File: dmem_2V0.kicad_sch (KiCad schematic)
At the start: 6 parts, among them J1 D15P33E4GV00LF, J10 7701-3, J11 7701-3

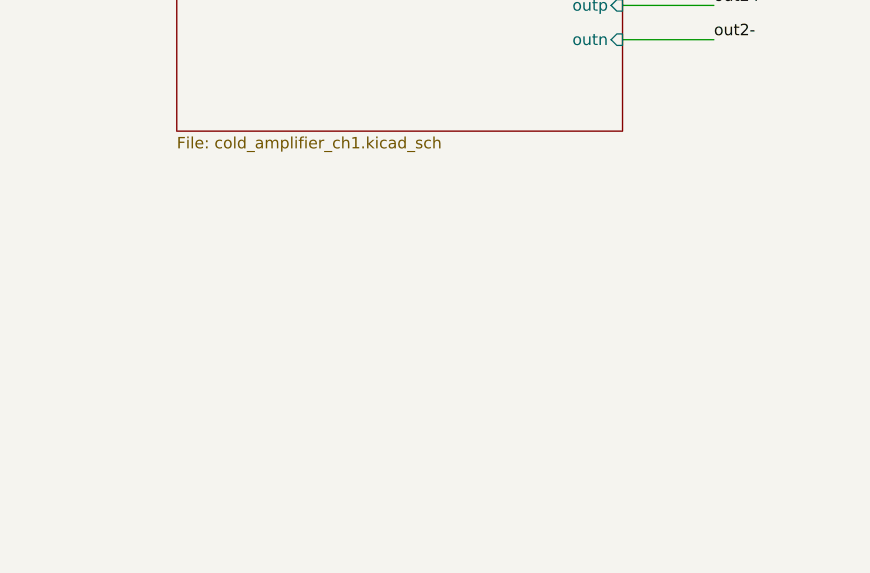
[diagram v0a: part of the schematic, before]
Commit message: Added jumpers to connect ground to mounting holes to ground
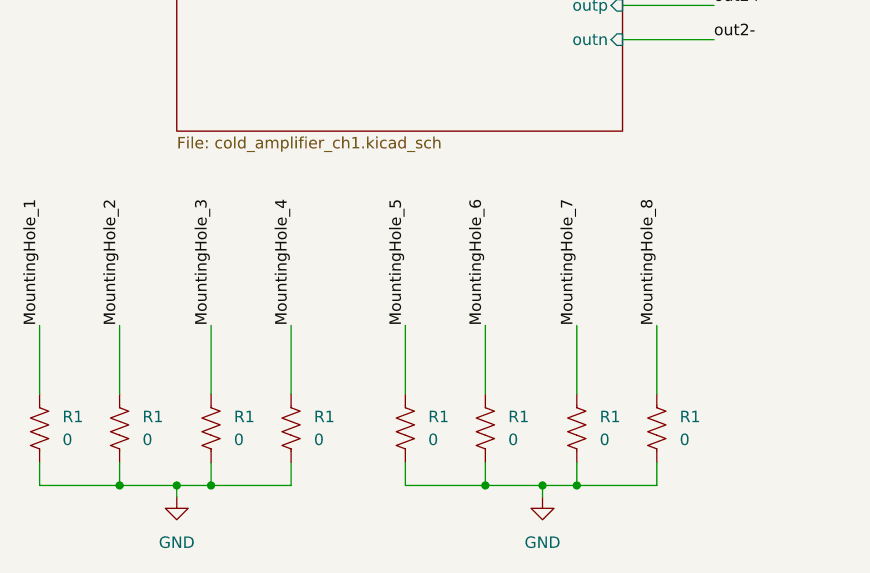
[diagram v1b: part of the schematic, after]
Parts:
- added R1 (x8): 0, Resistor_SMD:R_0805_2012Metric, symbol Device:R_US
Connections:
- net GND: now also R1.1, R1.1, R1.1, R1.1, R1.1, R1.1, R1.1, R1.1
- new net MountingHole_1: R1.2
- new net MountingHole_2: R1.2
- new net MountingHole_3: R1.2
- new net MountingHole_4: R1.2
- new net MountingHole_5: R1.2
- new net MountingHole_6: R1.2
- new net MountingHole_7: R1.2
- new net MountingHole_8: R1.2

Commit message: DMEM combination
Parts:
- added J12: D15S33E4GV00LF, User_footprints:AMPHENOL_D15S33E4GV00LF, symbol D15S33E4GV00LF:D15S33E4GV00LF
- added JP1: Jumper_2_Open, Resistor_SMD:R_1206_3216Metric, symbol Jumper:Jumper_2_Open
- added R1: 0, Resistor_SMD:R_0603_1608Metric, symbol Device:R_US
- J1: Digikey Part Number (none) -> 609-1492-ND; Part Number (none) -> D15P33E4GV00LF
- J10: Digikey Part Number (none) -> 36-7701-3-ND; Part Number  (none) -> 7701-3
- J11: footprint User_footprints:KEYSTONE_7701-3 -> 7701-3:KEYSTONE_7701-3; Description  (none) -> 4 Pin Screw Terminal, Power Tap 6-32 Through Hole; Digikey Part Number (none) -> 36-7701-3-ND; Part Number  (none) -> 7701-3
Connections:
- net +CE: now also J12.5
- net +CE_R: now also J12.14
- net GND: now also J12.15, J12.6, J12.7, J12.8, R1.1
- net MESH: now reaches J10.1_1 (1), J10.1_2 (1__1), J10.1_3 (1__2), J10.1_4 (1__3), JP2.1 (A), JP3.2 (B)
- net MESH: now also JP1.2 (B)
- net at JP3.1 (A): now also J1.S1 (SHIELD); no longer J1.16
- net out2_jumper-: now reaches J1.1
- net out2_jumper-: now also J12.3
- net out1_jumper+: now reaches J1.10
- net out1_jumper+: now also J12.12
- net out1_jumper-: now reaches J1.2
- net out1_jumper-: now also J12.4
- net out2_jumper+: now reaches J1.9
- net out2_jumper+: now also J12.11
- new net: J12.13, R1.2
- new net: J12.S1 (SHIELD), JP1.1 (A)
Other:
- moved on the sheet: JP3, R1

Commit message: Moved connectors SiPM flex connectorsto both sides; rectangular vias stitching pattern
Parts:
- J1: MANUFACTURER Amphenol ICC (FCI) -> (none); Manufacturer (none) -> Amphenol ICC (FCI)
- J10: MANUFACTURER Keystone Electronics -> (none); Manufacturer (none) -> Keystone Electronics
- J12: Digikey Part Number (none) -> 609-1498-ND; MANUFACTURER Amphenol -> (none); Manufacturer (none) -> Amphenol ICC (FCI); Part Number (none) -> D15S33E4GV00LF
- JP1, JP2, JP3: Digikey Part Number (none) -> RMCF1206ZT0R00CT-ND; Manufacturer (none) -> Stackpole Electronics Inc; Part Number (none) -> RMCF1206ZT0R00
- R1: Digikey Part Number (none) -> 749-MCU0805MZ0000ZP500CT-ND; Manufacturer (none) -> Vishay Beyschlag/Draloric/BC Components; Part Number (none) -> MCU0805MZ0000ZP500

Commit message: completed BOM list; replaced 47u with 33u capacitor
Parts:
- J1: MAXIMUM_PACKAGE_HEIGHT 12.96mm -> (none); PARTREV D -> (none); STANDARD Manufacturer recommendations -> (none)
- J10: footprint User_footprints:KEYSTONE_7701-3 -> 7701-3:KEYSTONE_7701-3; MAXIMUM_PACKAGE_HEIGHT 5.33 mm -> (none); PARTREV G -> (none); Part Number (none) -> 7701-3; Part Number  7701-3 -> (none); STANDARD Manufacturer Recommendations -> (none)
- J11: Description  4 Pin Screw Terminal, Power Tap 6-32 Through Hole -> (none); MANUFACTURER Keystone Electronics -> (none); MAXIMUM_PACKAGE_HEIGHT 5.33 mm -> (none); Manufacturer (none) -> Keystone Electronics; PARTREV G -> (none); Part Number (none) -> 7701-3; Part Number  7701-3 -> (none); STANDARD Manufacturer Recommendations -> (none)
- J12: footprint User_footprints:AMPHENOL_D15S33E4GV00LF -> D15S33E4GV00LF:AMPHENOL_D15S33E4GV00LF; PARTREV D -> (none); SNAPEDA_PN D15S33E4GV00LF -> (none); STANDARD Manufacturer Recommendations -> (none)
- R1: Digikey Part Number (none) -> 749-MCU0805MZ0000ZP500CT-ND; Manufacturer (none) -> Vishay Beyschlag/Draloric/BC Components; Part Number (none) -> MCU0805MZ0000ZP500
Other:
- moved on the sheet: J1
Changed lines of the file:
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@@
-    (stroke (width 0) (type default))
-  )
-  (wire (pts (xy 187.96 110.49) (xy 187.96 115.57))
     (stroke (width 0) (type default))
   )
@@
   )
   (wire (pts (xy 116.84 140.97) (xy 116.84 148.59))
+    (stroke (width 0) (type default))
+  )
+  (wire (pts (xy 187.96 111.76) (xy 187.96 115.57))
     (stroke (width 0) (type default))
   )
@@
       (effects (font (size 1.27 1.27)) hide)
     )
-    (property "PARTREV" "G" (at 251.46 143.51 0)
+    (property "Manufacturer" "Keystone Electronics" (at 251.46 138.43 0)
       (effects (font (size 1.27 1.27)) (justify bottom) hide)
     )
-    (property "STANDARD" "Manufacturer Recommendations" (at 251.46 143.51 0)
-      (effects (font (size 1.27 1.27)) (justify bottom) hide)
-    )
-    (property "MAXIMUM_PACKAGE_HEIGHT" "5.33 mm" (at 251.46 143.51 0)
-      (effects (font (size 1.27 1.27)) (justify bottom) hide)
-    )
-    (property "MANUFACTURER" "Keystone Electronics" (at 251.46 143.51 0)
-      (effects (font (size 1.27 1.27)) (justify bottom) hide)
-    )
-    (property "Part Number " "7701-3" (at 251.46 143.51 0)
+    (property "Part Number" "7701-3" (at 251.46 143.51 0)
       (effects (font (size 1.27 1.27)) hide)
     )
@@
       (effects (font (size 1.27 1.27)) hide)
     )
-    (property "Description " "4 Pin Screw Terminal, Power Tap 6-32 Through Hole" (at 251.46 143.51 0)
+    (property "Description" "4 Pin Screw Terminal, Power Tap 6-32 Through Hole" (at 251.46 143.51 0)
       (effects (font (size 1.27 1.27)) hide)
     )
@@
       (effects (font (size 1.27 1.27)))
     )
-    (property "Footprint" "User_footprints:AMPHENOL_D15S33E4GV00LF" (at 199.39 36.83 0)
+    (property "Footprint" "D15S33E4GV00LF:AMPHENOL_D15S33E4GV00LF" (at 199.39 36.83 0)
       (effects (font (size 1.27 1.27)) (justify bottom) hide)
     )
@@
       (effects (font (size 1.27 1.27)) hide)
     )
-    (property "PARTREV" "D" (at 200.66 55.88 0)
-      (effects (font (size 1.27 1.27)) (justify bottom) hide)
-    )
-    (property "STANDARD" "Manufacturer Recommendations" (at 172.72 44.45 0)
-      (effects (font (size 1.27 1.27)) (justify bottom) hide)
-    )
-    (property "SNAPEDA_PN" "D15S33E4GV00LF" (at 172.72 48.26 0)
-      (effects (font (size 1.27 1.27)) (justify bottom) hide)
-    )
-    (property "Manufacturer" "Amphenol ICC (FCI)" (at 180.34 41.91 0)
-      (effects (font (size 1.27 1.27)) (justify bottom) hide)
+    (property "Manufacturer" "Amphenol ICC (FCI)" (at 200.66 55.88 0)
+      (effects (font (size 1.27 1.27)) hide)
     )
     (property "Part Number" "D15S33E4GV00LF" (at 200.66 55.88 0)
@@
       (effects (font (size 1.27 1.27)) hide)
     )
+    (pin "10")
+    (pin "11")
+    (pin "12")
+    (pin "13")
+    (pin "14")
+    (pin "15")
+    (pin "S1")
     (pin "1")
     (pin "2")
@@
     (pin "8")
     (pin "9")
-    (pin "10")
-    (pin "11")
-    (pin "12")
-    (pin "13")
-    (pin "14")
-    (pin "15")
-    (pin "S1")
     (instances
       (project "dmem_2V0"
@@
       (effects (font (size 1.27 1.27)) hide)
     )
+    (property "Manufacturer" "Vishay Beyschlag/Draloric/BC Components" (at 231.14 55.88 0)
+      (effects (font (size 1.27 1.27)) hide)
+    )
+    (property "Part Number" "MCU0805MZ0000ZP500" (at 231.14 55.88 0)
+      (effects (font (size 1.27 1.27)) hide)
+    )
+    (property "Digikey Part Number" "749-MCU0805MZ0000ZP500CT-ND" (at 231.14 55.88 0)
+      (effects (font (size 1.27 1.27)) hide)
+    )
+    (property "Description" "0 Ohms Jumper Chip Resistor 0805 (2012 Metric) Anti-Sulfur, Automotive AEC-Q200 Thin Film" (at 231.14 55.88 0)
+      (effects (font (size 1.27 1.27)) hide)
+    )
     (pin "1")
     (pin "2")
@@
     )
   )
-  (symbol (lib_name "7701-3_1") (lib_id "7701-3:7701-3") (at 251.46 127 0) (unit 1)
+  (symbol (lib_id "7701-3:7701-3") (at 251.46 127 0) (unit 1)
     (in_bom yes) (on_board yes) (dnp no) (fields_autoplaced)
     (property "Reference" "J10" (at 257.81 129.54 0)
@@
       (effects (font (size 1.27 1.27)) (justify left))
     )
-    (property "Footprint" "User_footprints:KEYSTONE_7701-3" (at 251.46 127 0)
+    (property "Footprint" "7701-3:KEYSTONE_7701-3" (at 251.46 127 0)
       (effects (font (size 1.27 1.27)) (justify bottom) hide)
     )
@@
       (effects (font (size 1.27 1.27)) hide)
     )
-    (property "PARTREV" "G" (at 251.46 127 0)
+    (property "Manufacturer" "Keystone Electronics" (at 251.46 121.92 0)
       (effects (font (size 1.27 1.27)) (justify bottom) hide)
     )
-    (property "STANDARD" "Manufacturer Recommendations" (at 251.46 127 0)
-      (effects (font (size 1.27 1.27)) (justify bottom) hide)
-    )
-    (property "MAXIMUM_PACKAGE_HEIGHT" "5.33 mm" (at 251.46 127 0)
-      (effects (font (size 1.27 1.27)) (justify bottom) hide)
-    )
-    (property "Manufacturer" "Keystone Electronics" (at 251.46 127 0)
-      (effects (font (size 1.27 1.27)) (justify bottom) hide)
-    )
-    (property "Part Number " "7701-3" (at 251.46 127 0)
+    (property "Part Number" "7701-3" (at 251.46 127 0)
       (effects (font (size 1.27 1.27)) hide)
     )
@@
       (effects (font (size 1.27 1.27)) hide)
     )
-    (property "PARTREV" "D" (at 200.66 96.52 0)
-      (effects (font (size 1.27 1.27)) (justify bottom) hide)
-    )
-    (property "MAXIMUM_PACKAGE_HEIGHT" "12.96mm" (at 168.91 90.17 0)
-      (effects (font (size 1.27 1.27)) (justify bottom) hide)
-    )
-    (property "STANDARD" "Manufacturer recommendations" (at 177.8 80.01 0)
-      (effects (font (size 1.27 1.27)) (justify bottom) hide)
-    )
-    (property "Manufacturer" "Amphenol ICC (FCI)" (at 166.37 93.98 0)
-      (effects (font (size 1.27 1.27)) (justify bottom) hide)
-    )
-    (property "Part Number" "D15P33E4GV00LF" (at 214.63 80.01 0)
-      (effects (font (size 1.27 1.27)) hide)
-    )
-    (property "Digikey Part Number" "609-1492-ND" (at 209.55 76.2 0)
-      (effects (font (size 1.27 1.27)) hide)
-    )
-    (property "Description" "15 Position D-Sub Plug, Male Pins Connector" (at 215.9 72.39 0)
+    (property "Manufacturer" "Amphenol ICC (FCI)" (at 179.07 83.82 0)
+      (effects (font (size 1.27 1.27)) hide)
+    )
+    (property "Part Number" "D15P33E4GV00LF" (at 200.66 81.28 0)
+      (effects (font (size 1.27 1.27)) hide)
+    )
+    (property "Digikey Part Number" "609-1492-ND" (at 223.52 83.82 0)
+      (effects (font (size 1.27 1.27)) hide)
+    )
+    (property "Description" "15 Position D-Sub Plug, Male Pins Connector" (at 200.66 73.66 0)
       (effects (font (size 1.27 1.27)) hide)
     )
@@
       (effects (font (size 1.27 1.27)) hide)
     )
+    (property "Manufacturer" "Vishay Beyschlag/Draloric/BC Components" (at 231.14 99.06 0)
+      (effects (font (size 1.27 1.27)) hide)
+    )
+    (property "Part Number" "MCU0805MZ0000ZP500" (at 231.14 99.06 0)
+      (effects (font (size 1.27 1.27)) hide)
+    )
+    (property "Digikey Part Number" "749-MCU0805MZ0000ZP500CT-ND" (at 231.14 99.06 0)
+      (effects (font (size 1.27 1.27)) hide)
+    )
+    (property "Description" "0 Ohms Jumper Chip Resistor 0805 (2012 Metric) Anti-Sulfur, Automotive AEC-Q200 Thin Film" (at 231.14 99.06 0)
+      (effects (font (size 1.27 1.27)) hide)
+    )

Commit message: Adding test points and arrows to DB15s
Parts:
- added Vce1, Vce_r1: TestPoint, TestPoint:TestPoint_THTPad_1.0x1.0mm_Drill0.5mm, symbol Connector:TestPoint
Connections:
- net +CE: now also Vce1.1
- net +CE_R: now also Vce_r1.1
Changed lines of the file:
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@@
+    (stroke (width 0) (type default))
+  )
+  (wire (pts (xy 147.32 135.89) (xy 147.32 140.97))
     (stroke (width 0) (type default))
   )
@@
     (stroke (width 0) (type default))
   )
+  (wire (pts (xy 162.56 135.89) (xy 162.56 140.97))
+    (stroke (width 0) (type default))
+  )
   (wire (pts (xy 213.36 93.98) (xy 217.17 93.98))
     (stroke (width 0) (type default))
@@
     (effects (font (size 1.27 1.27)) (justify right bottom))
   )
+  (label "+CE_R" (at 162.56 140.97 180) (fields_autoplaced)
+    (effects (font (size 1.27 1.27)) (justify right bottom))
+  )
   (label "MountingHole_4" (at 76.2 140.97 90) (fields_autoplaced)
     (effects (font (size 1.27 1.27)) (justify left bottom))
@@
   )
   (label "out2-" (at 184.15 93.98 180) (fields_autoplaced)
+    (effects (font (size 1.27 1.27)) (justify right bottom))
+  )
+  (label "+CE" (at 147.32 140.97 180) (fields_autoplaced)
     (effects (font (size 1.27 1.27)) (justify right bottom))
   )
@@
     )
   )
+  (symbol (lib_id "Connector:TestPoint") (at 147.32 135.89 0) (unit 1)
+    (in_bom no) (on_board yes) (dnp no) (fields_autoplaced)
+    (property "Reference" "Vce1" (at 149.86 131.318 0)
+      (effects (font (size 1.27 1.27)) (justify left))
+    )
+    (property "Value" "TestPoint" (at 149.86 133.858 0)
+      (effects (font (size 1.27 1.27)) (justify left))
+    )
+    (property "Footprint" "TestPoint:TestPoint_THTPad_1.0x1.0mm_Drill0.5mm" (at 152.4 135.89 0)
+      (effects (font (size 1.27 1.27)) hide)
+    )
+    (property "Datasheet" "~" (at 152.4 135.89 0)
+      (effects (font (size 1.27 1.27)) hide)
+    )
+    (pin "1")
+    (instances
+      (project "dmem_2V0"
+        (path "/3e9c66f9-4dd4-413a-a9f0-4be475bcdd89"
+          (reference "Vce1") (unit 1)
+        )
+      )
+    )
+  )
   (symbol (lib_id "power:GND") (at 104.14 160.02 0) (unit 1)
     (in_bom yes) (on_board yes) (dnp no) (fields_autoplaced)
@@
         )
       )
+    )
+  )
+  (symbol (lib_id "Connector:TestPoint") (at 162.56 135.89 0) (unit 1)
+    (in_bom no) (on_board yes) (dnp no) (fields_autoplaced)
+    (property "Reference" "Vce_r1" (at 165.1 131.318 0)
+      (effects (font (size 1.27 1.27)) (justify left))
+    )
+    (property "Value" "TestPoint" (at 165.1 133.858 0)
+      (effects (font (size 1.27 1.27)) (justify left))
+    )
+    (property "Footprint" "TestPoint:TestPoint_THTPad_1.0x1.0mm_Drill0.5mm" (at 167.64 135.89 0)
+      (effects (font (size 1.27 1.27)) hide)
+    )
+    (property "Datasheet" "~" (at 167.64 135.89 0)
+      (effects (font (size 1.27 1.27)) hide)
+    )
+    (pin "1")
+    (instances
+      (project "dmem_2V0"
+        (path "/3e9c66f9-4dd4-413a-a9f0-4be475bcdd89"
+          (reference "Vce_r1") (unit 1)
+        )
+      )

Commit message: Solved error in netlist; input connector was in a mirror configuration; solved also DB15 error in netlist
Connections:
- net out1+: now also J1.4; no longer J1.12
- net out1-: now also J1.12; no longer J1.4
- net out1_jumper+: now also J1.2, J12.4; no longer J1.10, J12.12
- net out1_jumper-: now also J1.10, J12.12; no longer J1.2, J12.4
- net out2+: now also J1.3; no longer J1.11
- net out2-: now also J1.11; no longer J1.3
- net out2_jumper+: now also J1.1, J12.3; no longer J1.9, J12.11
- net out2_jumper-: now also J1.9, J12.11; no longer J1.1, J12.3
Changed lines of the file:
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@@
     (effects (font (size 1.27 1.27)) (justify left bottom))
   )
-  (label "out1_jumper+" (at 217.17 91.44 0) (fields_autoplaced)
+  (label "out1_jumper-" (at 217.17 91.44 0) (fields_autoplaced)
     (effects (font (size 1.27 1.27)) (justify left bottom))
   )
@@
     (effects (font (size 1.27 1.27)) (justify left bottom))
   )
-  (label "out2+" (at 217.17 93.98 0) (fields_autoplaced)
+  (label "out2-" (at 217.17 93.98 0) (fields_autoplaced)
     (effects (font (size 1.27 1.27)) (justify left bottom))
   )
@@
     (effects (font (size 1.27 1.27)) (justify right bottom))
   )
-  (label "out2-" (at 184.15 93.98 180) (fields_autoplaced)
+  (label "out2+" (at 184.15 93.98 180) (fields_autoplaced)
     (effects (font (size 1.27 1.27)) (justify right bottom))
   )
@@
     (effects (font (size 1.27 1.27)) (justify right bottom))
   )
-  (label "out2_jumper-" (at 184.15 50.8 180) (fields_autoplaced)
+  (label "out2_jumper+" (at 184.15 50.8 180) (fields_autoplaced)
     (effects (font (size 1.27 1.27)) (justify right bottom))
   )
-  (label "out1_jumper+" (at 217.17 53.34 0) (fields_autoplaced)
+  (label "out1_jumper-" (at 217.17 53.34 0) (fields_autoplaced)
     (effects (font (size 1.27 1.27)) (justify left bottom))
   )
@@
     (effects (font (size 1.27 1.27)) (justify left bottom))
   )
-  (label "out1+" (at 217.17 96.52 0) (fields_autoplaced)
+  (label "out1-" (at 217.17 96.52 0) (fields_autoplaced)
     (effects (font (size 1.27 1.27)) (justify left bottom))
   )
@@
     (effects (font (size 1.27 1.27)) (justify left bottom))
   )
-  (label "out2_jumper+" (at 217.17 88.9 0) (fields_autoplaced)
+  (label "out2_jumper-" (at 217.17 88.9 0) (fields_autoplaced)
     (effects (font (size 1.27 1.27)) (justify left bottom))
   )
-  (label "out2_jumper-" (at 184.15 88.9 180) (fields_autoplaced)
+  (label "out2_jumper+" (at 184.15 88.9 180) (fields_autoplaced)
     (effects (font (size 1.27 1.27)) (justify right bottom))
   )
@@
     (effects (font (size 1.27 1.27)) (justify left bottom))
   )
-  (label "out1_jumper-" (at 184.15 53.34 180) (fields_autoplaced)
+  (label "out1_jumper+" (at 184.15 53.34 180) (fields_autoplaced)
     (effects (font (size 1.27 1.27)) (justify right bottom))
   )
@@
     (effects (font (size 1.27 1.27)) (justify left bottom))
   )
-  (label "out2_jumper+" (at 217.17 50.8 0) (fields_autoplaced)
+  (label "out2_jumper-" (at 217.17 50.8 0) (fields_autoplaced)
     (effects (font (size 1.27 1.27)) (justify left bottom))
   )
-  (label "out1_jumper-" (at 184.15 91.44 180) (fields_autoplaced)
+  (label "out1_jumper+" (at 184.15 91.44 180) (fields_autoplaced)
     (effects (font (size 1.27 1.27)) (justify right bottom))
   )
@@
     (effects (font (size 1.27 1.27)) (justify left bottom))
   )
-  (label "out1-" (at 184.15 96.52 180) (fields_autoplaced)
+  (label "out1+" (at 184.15 96.52 180) (fields_autoplaced)
     (effects (font (size 1.27 1.27)) (justify right bottom))
   )

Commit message: Version tested at coldbox March 2026
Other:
- note added: "18/12/2024"
- note added: "2"
- note added: "DMEM V2.0 - Top level"
- note added: "Esteban Cristaldo Claudio Gotti"
- note added: "INFN Milano-Bicocca"
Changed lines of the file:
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@@
     (stroke (width 0) (type default))
+  )
+  (text "Esteban Cristaldo \nClaudio Gotti\n" (at 177.8 171.45 0)
+    (effects (font (size 1.27 1.27)) (justify left bottom))
+  )
+  (text "2\n" (at 267.97 194.31 0)
+    (effects (font (size 1.27 1.27)) (justify left bottom))
+  )
+  (text "DMEM V2.0 - Top level" (at 187.96 190.5 0)
+    (effects (font (size 1.27 1.27)) (justify left bottom))
+  )
+  (text "INFN Milano-Bicocca\n" (at 177.8 173.99 0)
+    (effects (font (size 1.27 1.27)) (justify left bottom))
+  )
+  (text "18/12/2024\n" (at 205.74 194.31 0)
+    (effects (font (size 1.27 1.27)) (justify left bottom))
   )
   (label "+CE" (at 121.92 90.17 0) (fields_autoplaced)
